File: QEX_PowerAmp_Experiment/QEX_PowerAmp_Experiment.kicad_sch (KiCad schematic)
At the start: 73 parts, among them J1 Key In, J10 Conn_01x02, J11 SMA, J12 Conn_01x02, J2 Key In, J3 Conn_01x02, J4 Conn_01x02, J5 SMA, J6 Conn_01x02, J7 Conn_01x02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

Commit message: Starting layout work
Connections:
- net k1: now reaches C4.1, R2.2, R4.1
- net k3: now reaches C4.2, R6.1, U8.1, U8.2 (-)
- net G1: now reaches Q2.4 (G), U5.5 (OUT)
- net k4: now reaches C12.1, R6.2, R7.1
- net k5: now reaches C13.1, R7.2, U8.5 (+)
- net k9: now reaches J9.2 (Pin_2), J9.3 (Pin_3), R13.1, RV1.1, RV1.2
- net cm1: now reaches Q3.2 (B1), Q3.5 (B2), Q3.6 (C1), R13.2
- net k6: now reaches C12.2, U8.10 (+), U8.6 (-), U8.7
- net k2: now reaches C6.1, R4.2, U8.3 (+)
- net sw: now reaches C21.2, L3.1, U7.2 (SW)
- net th_out: now reaches J10.1 (Pin_1), R17.2, U8.14
- net D1: now reaches L1.3, L2.1, Q2.5 (D)
- net D2: now reaches L1.2, L2.3, Q2.6 (D)
- net cm2: now reaches Q3.3 (C2), R18.1
- net cs_out: now reaches J4.1 (Pin_1), U2.1
- net keyIn: now reaches J1.1 (In), J2.1 (Pin_1), R1.1, R2.1
- net base: now reaches C8.1, D1.1 (K), Q1.1 (B), R5.2
- net th1: now reaches R15.2, TH1.1, U8.12 (+)
- net fb: now reaches R18.2, R19.1, R20.1, U7.4 (FB)
- net G2: now reaches Q2.2 (G), U6.5 (OUT)
- net k8: now reaches J9.1 (Pin_1), R11.2, RV1.3, U8.8
- net k7: now reaches R10.1, R11.1, U8.9 (-)
- net VDD_PWR: now reaches J12.2 (Pin_2), L1.1, L1.4
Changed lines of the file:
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@@
+		)
+	)
+	(label "cm2"
+		(at 298.45 66.04 0)
+		(effects
+			(font
+				(size 1.27 1.27)
+			)
+			(justify left bottom)
 		)
 	)
@@
 		)
 	)
+	(label "k3"
+		(at 120.65 48.26 0)
+		(effects
+			(font
+				(size 1.27 1.27)
+			)
+			(justify left bottom)
+		)
+	)
 	(label "sw_enable"
 		(at 257.81 24.13 0)
@@
 		)
 	)
+	(label "G2"
+		(at 245.11 181.61 0)
+		(effects
+			(font
+				(size 1.27 1.27)
+			)
+			(justify left bottom)
+		)
+	)
+	(label "k2"
+		(at 92.71 50.8 0)
+		(effects
+			(font
+				(size 1.27 1.27)
+			)
+			(justify left bottom)
+		)
+	)
+	(label "k9"
+		(at 257.81 66.04 0)
+		(effects
+			(font
+				(size 1.27 1.27)
+			)
+			(justify left bottom)
+		)
+	)
+	(label "G1"
+		(at 245.11 162.56 0)
+		(effects
+			(font
+				(size 1.27 1.27)
+			)
+			(justify left bottom)
+		)
+	)
+	(label "keyIn"
+		(at 48.26 50.8 0)
+		(effects
+			(font
+				(size 1.27 1.27)
+			)
+			(justify left bottom)
+		)
+	)
+	(label "cm1"
+		(at 283.21 66.04 0)
+		(effects
+			(font
+				(size 1.27 1.27)
+			)
+			(justify left bottom)
+		)
+	)
+	(label "k5"
+		(at 160.02 48.26 0)
+		(effects
+			(font
+				(size 1.27 1.27)
+			)
+			(justify left bottom)
+		)
+	)
+	(label "cs_out"
+		(at 114.3 238.76 0)
+		(effects
+			(font
+				(size 1.27 1.27)
+			)
+			(justify left bottom)
+		)
+	)
+	(label "D1"
+		(at 288.29 154.94 0)
+		(effects
+			(font
+				(size 1.27 1.27)
+			)
+			(justify left bottom)
+		)
+	)
+	(label "VDD_PWR"
+		(at 298.45 144.78 0)
+		(effects
+			(font
+				(size 1.27 1.27)
+			)
+			(justify left bottom)
+		)
+	)
+	(label "sw"
+		(at 302.26 33.02 0)
+		(effects
+			(font
+				(size 1.27 1.27)
+			)
+			(justify left bottom)
+		)
+	)
+	(label "th_out"
+		(at 300.99 121.92 0)
+		(effects
+			(font
+				(size 1.27 1.27)
+			)
+			(justify left bottom)
+		)
+	)
+	(label "k7"
+		(at 182.88 50.8 0)
+		(effects
+			(font
+				(size 1.27 1.27)
+			)
+			(justify left bottom)
+		)
+	)
 	(label "~{rf_enable}"
 		(at 173.99 208.28 0)
@@
 		)
 	)
+	(label "k4"
+		(at 142.24 48.26 0)
+		(effects
+			(font
+				(size 1.27 1.27)
+			)
+			(justify left bottom)
+		)
+	)
+	(label "D2"
+		(at 288.29 190.5 0)
+		(effects
+			(font
+				(size 1.27 1.27)
+			)
+			(justify left bottom)
+		)
+	)
+	(label "k6"
+		(at 184.15 45.72 0)
+		(effects
+			(font
+				(size 1.27 1.27)
+			)
+			(justify left bottom)
+		)
+	)
+	(label "th1"
+		(at 270.51 119.38 0)
+		(effects
+			(font
+				(size 1.27 1.27)
+			)
+			(justify left bottom)
+		)
+	)
+	(label "fb"
+		(at 299.72 39.37 0)
+		(effects
+			(font
+				(size 1.27 1.27)
+			)
+			(justify left bottom)
+		)
+	)
 	(label "rfd+"
 		(at 191.77 165.1 0)
 		(effects
 			(font
+				(size 1.27 1.27)
+			)
+			(justify left bottom)
+		)
+	)
+	(label "base"
+		(at 91.44 120.65 0)
+		(effects
+			(font
+				(size 1.27 1.27)
+			)
+			(justify left bottom)
+		)
+	)
+	(label "k1"
+		(at 73.66 50.8 0)
+		(effects
+			(font
+				(size 1.27 1.27)
+			)
+			(justify left bottom)
+		)
+	)
+	(label "k8"
+		(at 226.06 66.04 0)
+		(effects
+			(font

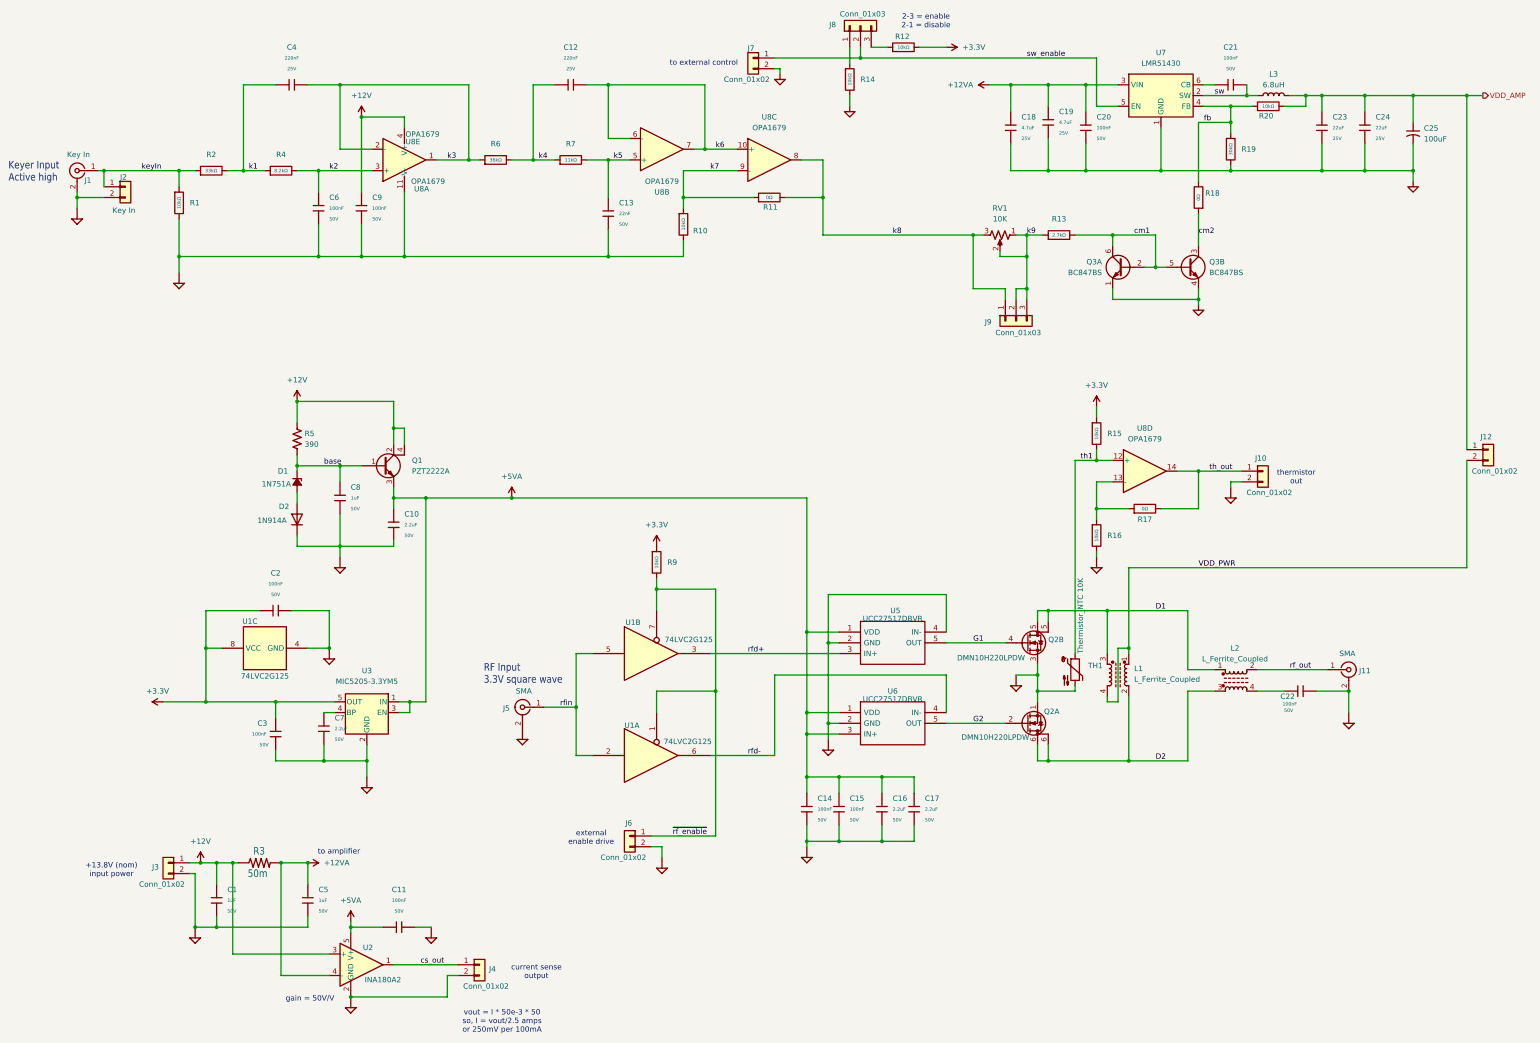
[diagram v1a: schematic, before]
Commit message: Starting layout connections
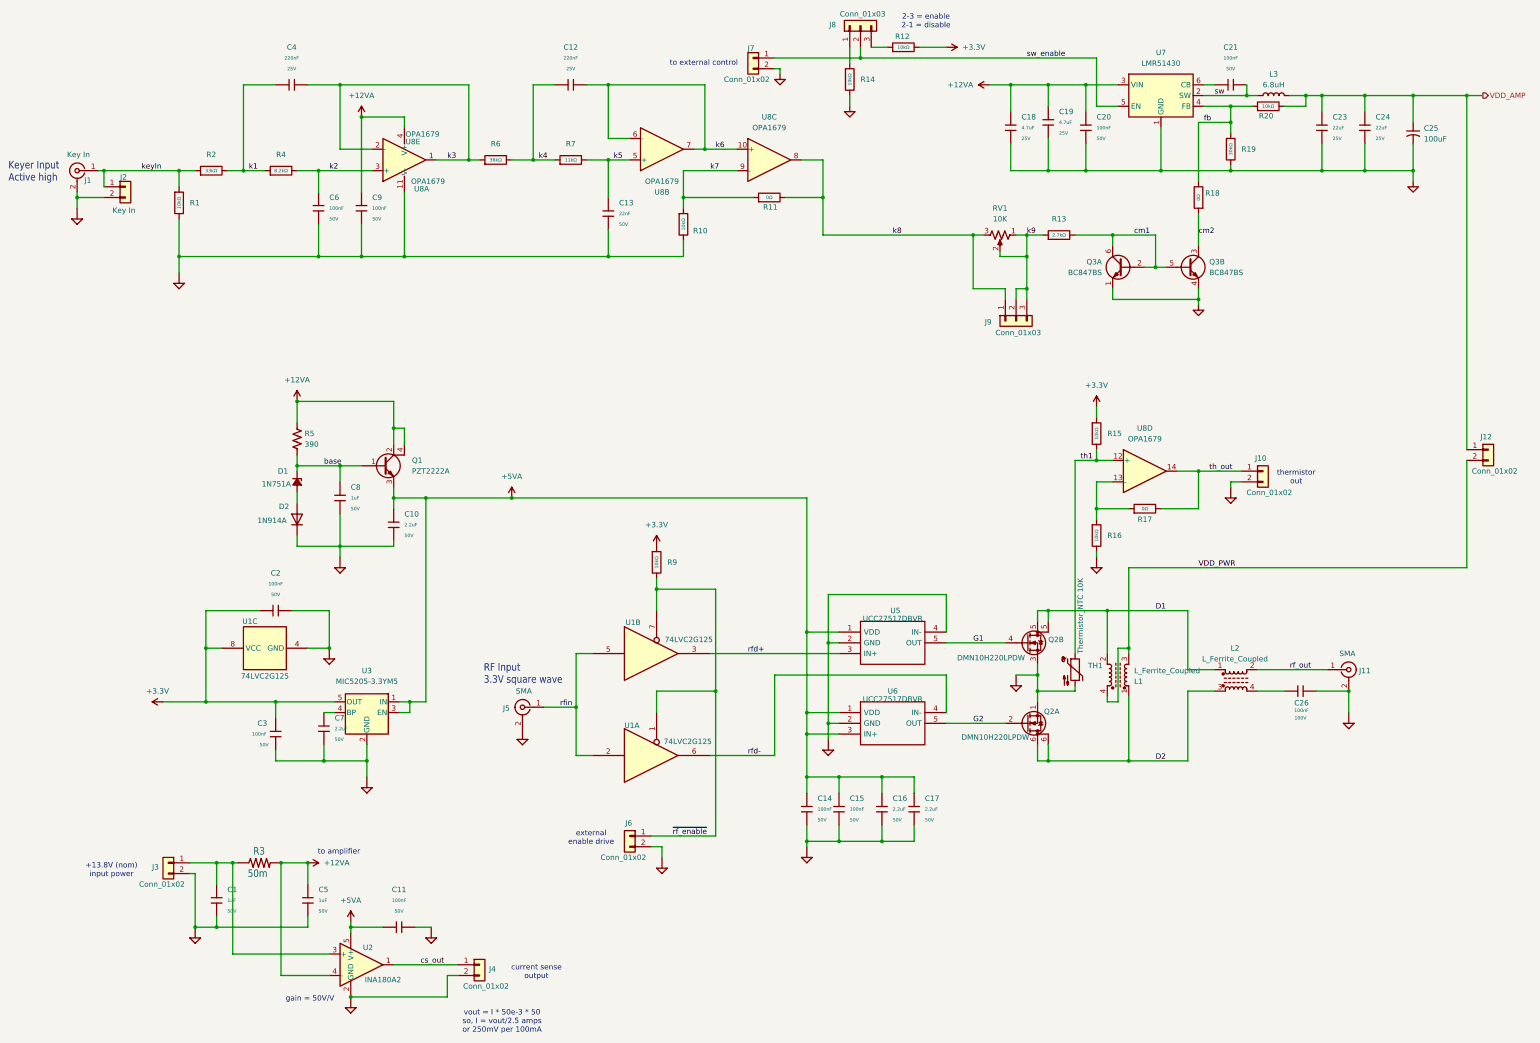
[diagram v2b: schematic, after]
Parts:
- removed C22: 100nF, PCM_JLCPCB:C_0603, symbol PCM_JLCPCB-Capacitors:0603,100nF
- added C26: 100nF, PCM_JLCPCB:C_0805, symbol PCM_JLCPCB-Capacitors:0805,100nF
- L1: symbol Device:L_Ferrite_Coupled -> Device:L_Ferrite_Coupled_1342; now in the parts list
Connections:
- net +12VA: now also C9.1, Q1.2 (C), Q1.4 (C), R5.1, U8.4 (V+)
- net D1: now also L1.2; no longer L1.3
- net D2: now also L1.1; no longer L1.2
- net GND: now also C26.2
- net VDD_PWR: now also L1.3; no longer L1.1
- net at L2.4: now also C26.1
- removed net +12V: C1.1, C9.1, J3.1 (Pin_1), Q1.2 (C), Q1.4 (C), R3.1, R5.1, U2.3 (+), U8.4 (V+)
- new net: C1.1, J3.1 (Pin_1), R3.1, U2.3 (+)

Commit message: Clean DRC
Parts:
- D1, D2, J1, J10, J11, J12, J2, J3, J4, J5, J6, J7, J8, J9, L2, L3, R5, RV1: now not fitted
- L1: now not fitted; now left out of the parts list
- R3, TH1: now in the parts list
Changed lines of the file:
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@@
 		(exclude_from_sim no)
 		(in_bom yes)
-		(on_board yes)
+		(on_board no)
 		(dnp no)
 		(property "Reference" "R12"
@@
 		(exclude_from_sim no)
 		(in_bom yes)
-		(on_board yes)
+		(on_board no)
 		(dnp no)
 		(property "Reference" "U5"
@@
 		(exclude_from_sim no)
 		(in_bom no)
-		(on_board yes)
-		(dnp no)
+		(on_board no)
+		(dnp yes)
 		(property "Reference" "J6"
 			(at 163.576 205.232 0)
@@
 		(exclude_from_sim no)
 		(in_bom yes)
-		(on_board yes)
+		(on_board no)
 		(dnp no)
 		(fields_autoplaced yes)
@@
 		(exclude_from_sim no)
 		(in_bom yes)
-		(on_board yes)
+		(on_board no)
 		(dnp no)
 		(fields_autoplaced yes)
@@
 		(exclude_from_sim no)
 		(in_bom yes)
-		(on_board yes)
+		(on_board no)
 		(dnp no)
 		(property "Reference" "U8"
@@
 		(exclude_from_sim no)
 		(in_bom no)
-		(on_board yes)
-		(dnp no)
+		(on_board no)
+		(dnp yes)
 		(fields_autoplaced yes)
 		(property "Reference" "L3"
@@
 		(exclude_from_sim no)
 		(in_bom yes)
-		(on_board yes)
+		(on_board no)
 		(dnp no)
 		(property "Reference" "R17"
@@
 		(exclude_from_sim no)
 		(in_bom no)
-		(on_board yes)
-		(dnp no)
+		(on_board no)
+		(dnp yes)
 		(fields_autoplaced yes)
 		(property "Reference" "L2"
@@
 		(exclude_from_sim no)
 		(in_bom yes)
-		(on_board yes)
+		(on_board no)
 		(dnp no)
 		(fields_autoplaced yes)
@@
 		(exclude_from_sim no)
 		(in_bom no)
-		(on_board yes)
-		(dnp no)
+		(on_board no)
+		(dnp yes)
 		(property "Reference" "J10"
 			(at 313.182 118.872 0)
@@
 		(exclude_from_sim no)
 		(in_bom no)
-		(on_board yes)
-		(dnp no)
+		(on_board no)
+		(dnp yes)
 		(property "Reference" "J3"
 			(at 51.562 215.646 0)
@@
 		(exclude_from_sim no)
 		(in_bom no)
-		(on_board yes)
-		(dnp no)
+		(on_board no)
+		(dnp yes)
 		(property "Reference" "J4"
 			(at 131.318 239.776 0)
@@
 		(exclude_from_sim no)
 		(in_bom no)
-		(on_board yes)
-		(dnp no)
+		(on_board no)
+		(dnp yes)
 		(property "Reference" "J7"
 			(at 192.532 21.844 0)
@@
 		(exclude_from_sim no)
 		(in_bom yes)
-		(on_board yes)
+		(on_board no)
 		(dnp no)
 		(fields_autoplaced yes)
@@
 		(exclude_from_sim no)
 		(in_bom no)
-		(on_board yes)
-		(dnp no)
+		(on_board no)
+		(dnp yes)
 		(property "Reference" "J8"
 			(at 211.836 16.256 90)
@@
 		(exclude_from_sim no)
 		(in_bom yes)
-		(on_board yes)
+		(on_board no)
 		(dnp no)
 		(property "Reference" "Q2"
@@
 		(exclude_from_sim no)
 		(in_bom yes)
-		(on_board yes)
+		(on_board no)
 		(dnp no)
 		(fields_autoplaced yes)
@@
 		(unit 1)
 		(exclude_from_sim no)
-		(in_bom no)
-		(on_board yes)
+		(in_bom yes)
+		(on_board no)
 		(dnp no)
 		(property "Reference" "R3"
@@
 		(exclude_from_sim no)
 		(in_bom yes)
-		(on_board yes)
+		(on_board no)
 		(dnp no)
 		(fields_autoplaced yes)
@@
 		(exclude_from_sim no)
 		(in_bom yes)
-		(on_board yes)
+		(on_board no)
 		(dnp no)
 		(fields_autoplaced yes)
@@
 		(exclude_from_sim no)
 		(in_bom no)
-		(on_board yes)
-		(dnp no)
+		(on_board no)
+		(dnp yes)
 		(property "Reference" "J2"
 			(at 43.18 52.324 0)
@@
 		(exclude_from_sim no)
 		(in_bom no)
-		(on_board yes)
-		(dnp no)
+		(on_board no)
+		(dnp yes)
 		(property "Reference" "J1"
 			(at 35.56 53.086 0)
@@
 		(exclude_from_sim no)
 		(in_bom yes)
-		(on_board yes)
+		(on_board no)
 		(dnp no)
 		(property "Reference" "U1"
@@
 		(exclude_from_sim no)
 		(in_bom no)
-		(on_board yes)
-		(dnp no)
+		(on_board no)
+		(dnp yes)
 		(property "Reference" "J5"
 			(at 134.62 178.054 0)
@@
 		(exclude_from_sim no)
 		(in_bom yes)
-		(on_board yes)
+		(on_board no)
 		(dnp no)
 		(property "Reference" "U6"
@@
 		(exclude_from_sim no)
 		(in_bom yes)
-		(on_board yes)
+		(on_board no)
 		(dnp no)
 		(property "Reference" "U8"
@@
 		(exclude_from_sim no)
 		(in_bom yes)
-		(on_board yes)
+		(on_board no)
 		(dnp no)
 		(fields_autoplaced yes)
@@
 		(exclude_from_sim no)
 		(in_bom yes)
-		(on_board yes)
+		(on_board no)
 		(dnp no)
 		(property "Reference" "R10"
@@
 		(exclude_from_sim no)
 		(in_bom yes)
-		(on_board yes)
+		(on_board no)
 		(dnp no)
 		(property "Reference" "U8"
@@
 		(exclude_from_sim no)
 		(in_bom no)
-		(on_board yes)
-		(dnp no)
+		(on_board no)
+		(dnp yes)
 		(property "Reference" "J12"
 			(at 366.522 113.792 0)
@@
 		(exclude_from_sim no)
 		(in_bom no)
-		(on_board yes)
-		(dnp no)
+		(on_board no)
+		(dnp yes)
 		(property "Reference" "J9"
 			(at 248.666 86.614 90)
@@
 		(exclude_from_sim no)
 		(in_bom yes)
-		(on_board yes)
+		(on_board no)
 		(dnp no)
 		(property "Reference" "U1"
@@
 		(unit 1)
 		(exclude_from_sim no)
-		(in_bom yes)
-		(on_board yes)
-		(dnp no)
+		(in_bom no)
+		(on_board no)
+		(dnp yes)
 		(property "Reference" "L1"
 			(at 283.21 171.7041 90)
@@
 		(exclude_from_sim no)
 		(in_bom yes)
-		(on_board yes)
+		(on_board no)
 		(dnp no)
 		(fields_autoplaced yes)
@@
 		(exclude_from_sim no)
 		(in_bom yes)
-		(on_board yes)
+		(on_board no)
 		(dnp no)
 		(property "Reference" "U2"
@@
 		(exclude_from_sim no)
 		(in_bom no)
-		(on_board yes)
-		(dnp no)
+		(on_board no)
+		(dnp yes)
 		(property "Reference" "D1"
 			(at 80.518 121.92 90)
@@
 		(exclude_from_sim no)
 		(in_bom yes)
-		(on_board yes)
+		(on_board no)
 		(dnp no)
 		(property "Reference" "U1"
@@
 		(exclude_from_sim no)
 		(in_bom yes)
-		(on_board yes)
+		(on_board no)
 		(dnp no)
 		(fields_autoplaced yes)
@@
 		(exclude_from_sim no)
 		(in_bom yes)
-		(on_board yes)
+		(on_board no)
 		(dnp no)
 		(fields_autoplaced yes)
@@
 		(exclude_from_sim no)
 		(in_bom yes)
-		(on_board yes)
+		(on_board no)
 		(dnp no)
 		(property "Reference" "R11"
@@
 		(exclude_from_sim no)
 		(in_bom no)
-		(on_board yes)
-		(dnp no)
+		(on_board no)
+		(dnp yes)
 		(property "Reference" "J11"
 			(at 337.82 169.164 0)
@@
 		(exclude_from_sim no)
 		(in_bom yes)
-		(on_board yes)
+		(on_board no)
 		(dnp no)
 		(property "Reference" "R20"
@@
 		(exclude_from_sim no)
 		(in_bom yes)
-		(on_board yes)
+		(on_board no)
 		(dnp no)
 		(fields_autoplaced yes)
@@
 		(exclude_from_sim no)
 		(in_bom yes)
-		(on_board yes)
+		(on_board no)
 		(dnp no)
 		(fields_autoplaced yes)
@@
 		(exclude_from_sim no)
 		(in_bom yes)
-		(on_board yes)
+		(on_board no)
 		(dnp no)
 		(property "Reference" "Q2"
@@
 		(exclude_from_sim no)
 		(in_bom yes)
-		(on_board yes)
+		(on_board no)
 		(dnp no)
 		(fields_autoplaced yes)
@@
 		(unit 1)
 		(exclude_from_sim no)
-		(in_bom no)
-		(on_board yes)
+		(in_bom yes)
+		(on_board no)
 		(dnp no)
 		(property "Reference" "TH1"
@@
 		(exclude_from_sim no)
 		(in_bom no)
-		(on_board yes)
-		(dnp no)
+		(on_board no)
+		(dnp yes)
 		(fields_autoplaced yes)
 		(property "Reference" "R5"
@@
 		(exclude_from_sim no)
 		(in_bom yes)
-		(on_board yes)
+		(on_board no)
 		(dnp no)
 		(fields_autoplaced yes)
@@
 		(exclude_from_sim no)
 		(in_bom yes)
-		(on_board yes)
+		(on_board no)
 		(dnp no)
 		(property "Reference" "Q3"
@@
 		(exclude_from_sim no)
 		(in_bom no)
-		(on_board yes)
-		(dnp no)
+		(on_board no)
+		(dnp yes)
 		(fields_autoplaced yes)
 		(property "Reference" "RV1"
@@
 		(exclude_from_sim no)
 		(in_bom yes)
-		(on_board yes)
+		(on_board no)
 		(dnp no)
 		(property "Reference" "R18"
@@
 		(exclude_from_sim no)
 		(in_bom no)
-		(on_board yes)
-		(dnp no)
+		(on_board no)
+		(dnp yes)
 		(property "Reference" "D2"
 			(at 80.772 130.302 90)
@@
 		(exclude_from_sim no)
 		(in_bom yes)
-		(on_board yes)
+		(on_board no)
 		(dnp no)
 		(property "Reference" "U3"
@@
 		(exclude_from_sim no)
 		(in_bom yes)
-		(on_board yes)
+		(on_board no)
 		(dnp no)
 		(fields_autoplaced yes)

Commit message: Refining layout
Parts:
- R3: JLCPCB (none) -> C858613
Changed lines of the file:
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@@
+			)
+		)
+		(property "JLCPCB" "C858613"
+			(at 76.2 214.63 0)
+			(effects
+				(font
+					(size 1.27 1.27)
+				)
+				(hide yes)
 			)
 		)
